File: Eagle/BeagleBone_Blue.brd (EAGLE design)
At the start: 86.4 x 54.6 mm, 128 parts, among them M1 JST_ZH_2, M2 JST_ZH_2, M3 JST_ZH_2, M4 JST_ZH_2, Q3 MOSFET-N, Q4 MOSFET-P, U1 MPU-9250

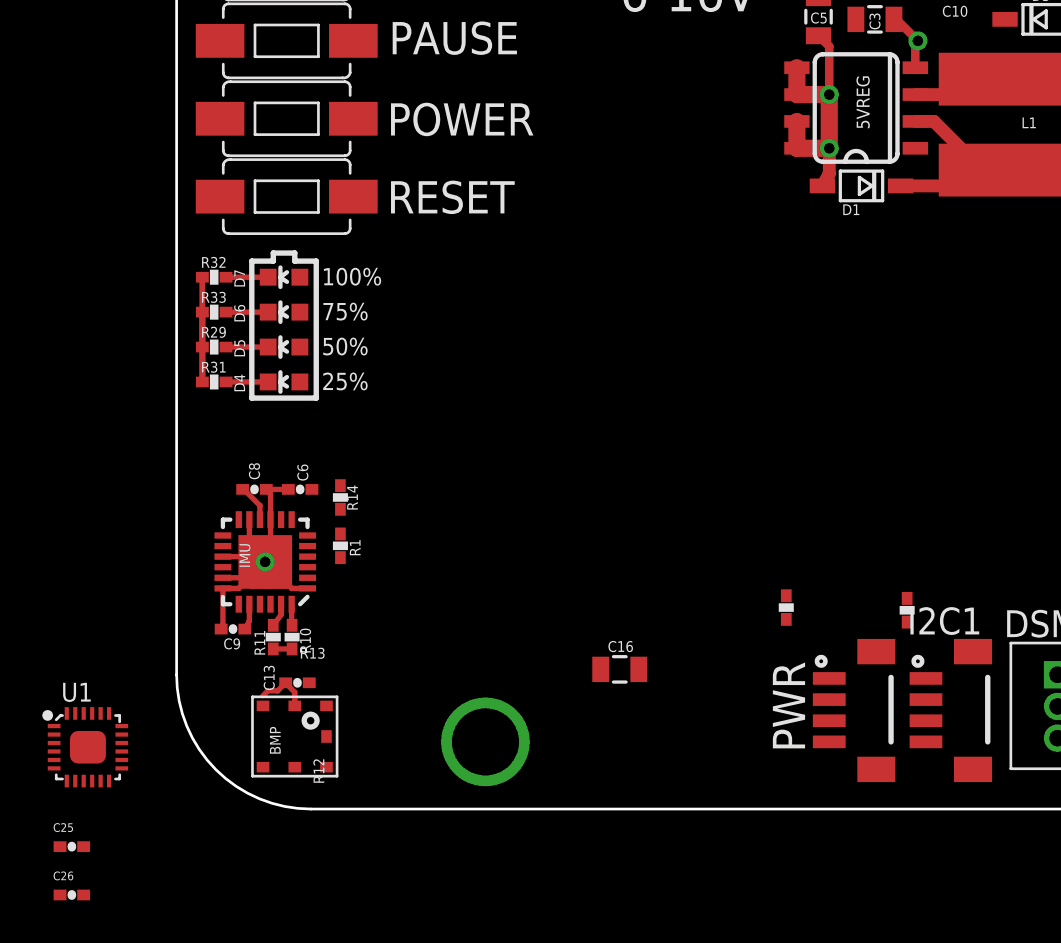
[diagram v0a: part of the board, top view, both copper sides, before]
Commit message: working on ERCs
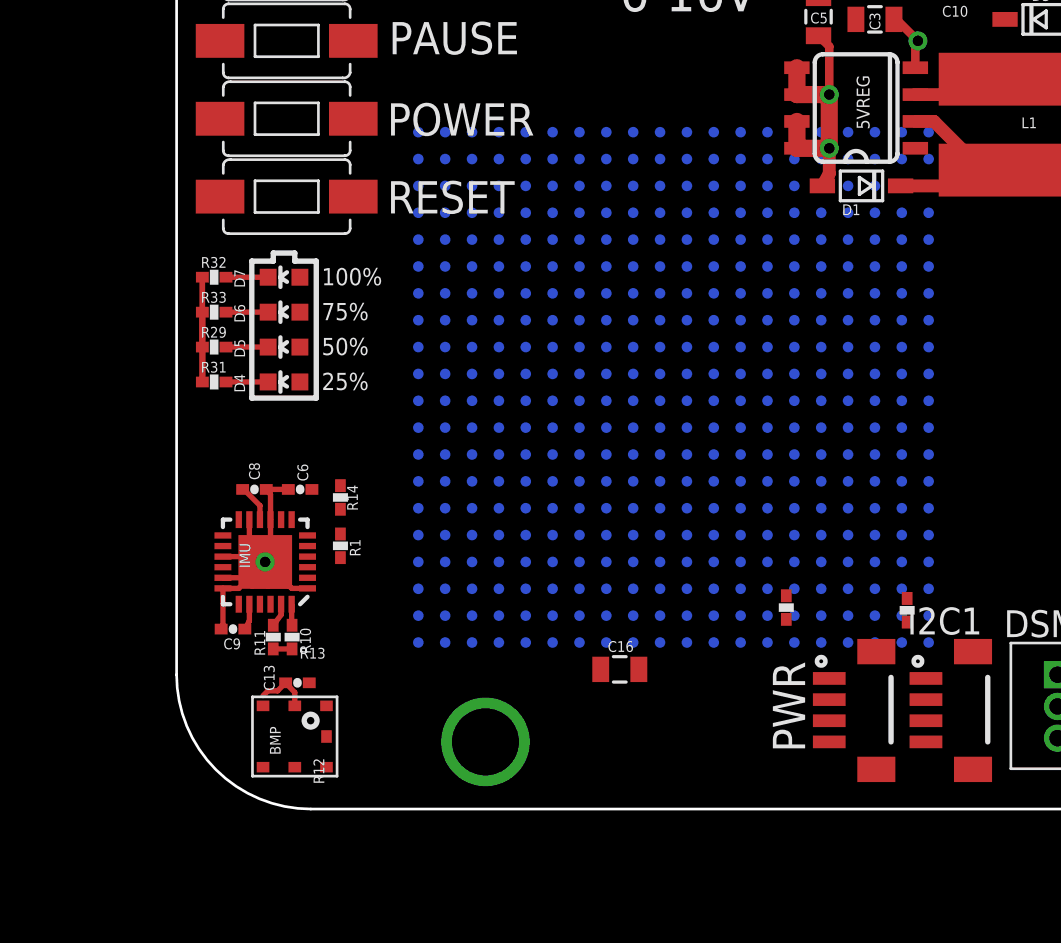
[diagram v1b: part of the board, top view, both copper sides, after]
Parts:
- removed C25, C26: 0.1uF, Strawson_Eagle_Lib:0402-CAP
- removed U1: MPU-9250, Strawson_Eagle_Lib:QFN24G-0.4-3X3MM
- added SIP: (no value), BeagleBone_Blue:OSD3358
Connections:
- removed net N$70: C26.2, U1.10
- net 3.3V: no longer C25.1, U1.1, U1.13, U1.8
- net GND: no longer C25.2, C26.1, U1.18, U1.20, U1.25, U1.9
- net I2C2_SCL: no longer U1.23
- net I2C2_SDA: no longer U1.24
- net IMU_INT: no longer U1.12

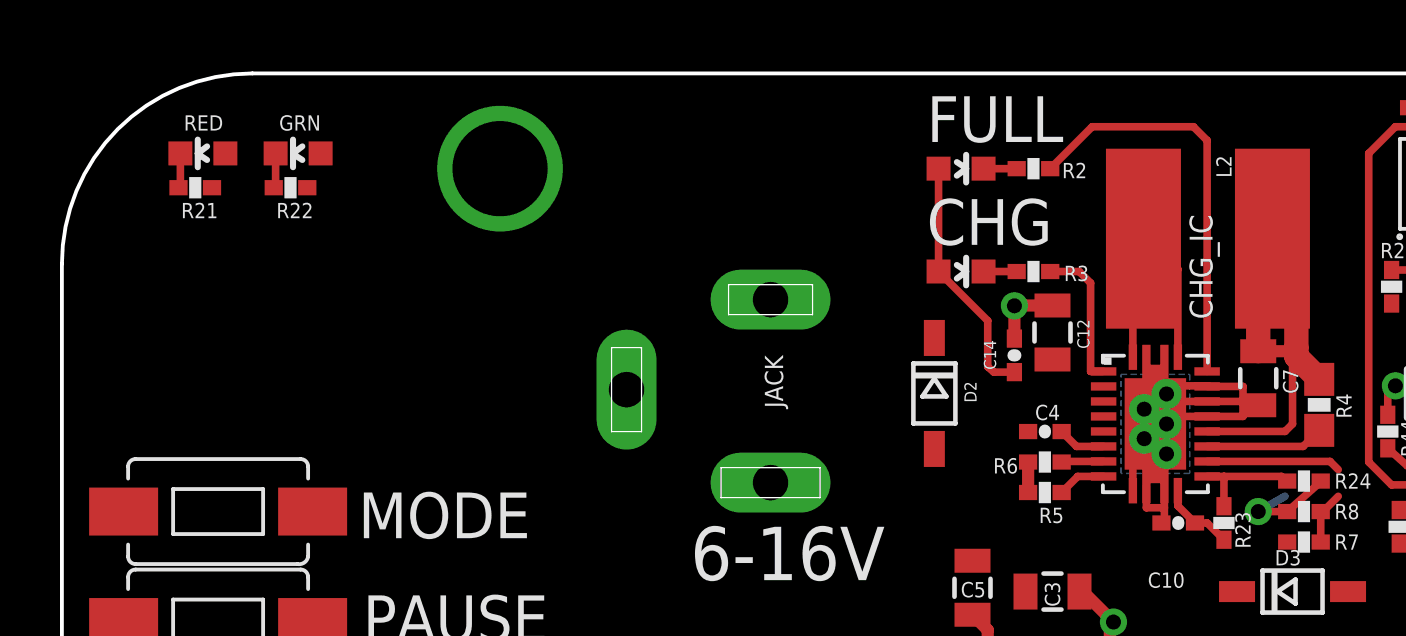
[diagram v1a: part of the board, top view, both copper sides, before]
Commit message: Fix some ERCs
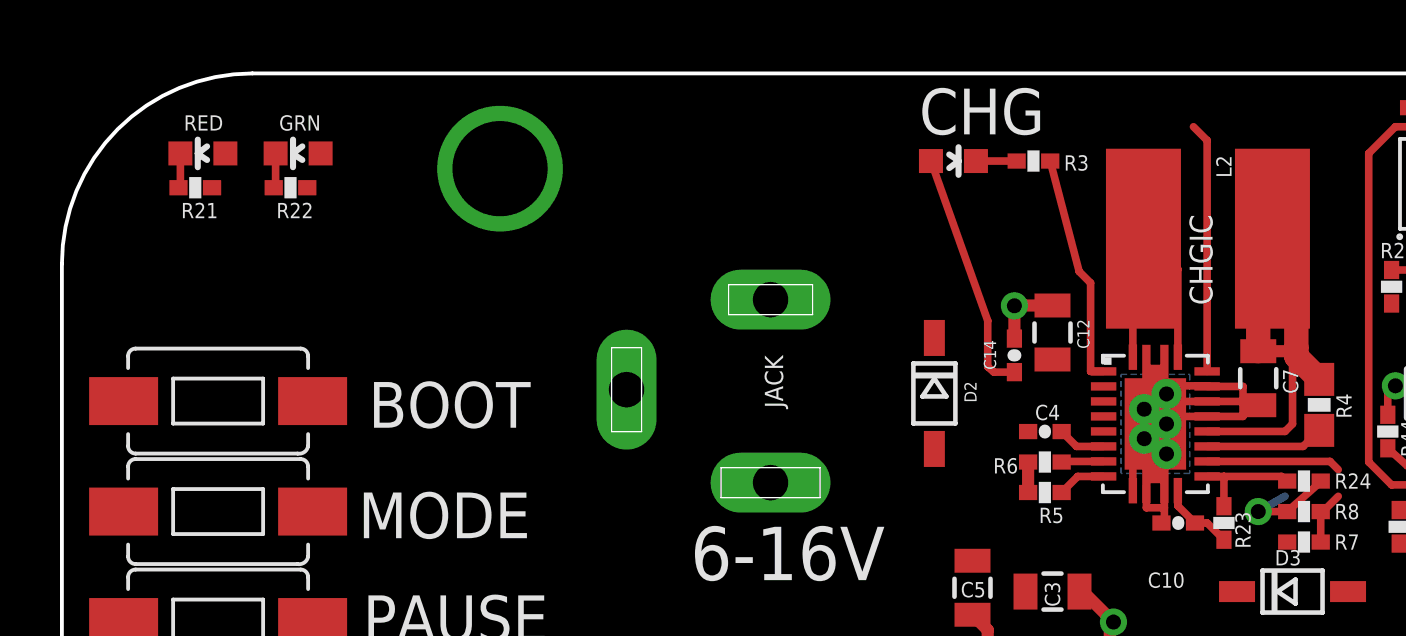
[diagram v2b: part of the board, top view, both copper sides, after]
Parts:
- removed FULL: GRN, SparkFun-LED:LED-0603
- removed R2: 698, Strawson_Eagle_Lib:0402-RES
- added BOOT: SWITCH-MOMENTARY-2-SMD-1101NE, SparkFun-Electromechanical:TACTILE-SWITCH-1101NE
- moved CHG 3.69 mm to (29.7, 51.7)
- moved R3 3.68 mm to (32.4, 51.7)
- renumbered CHG_IC to CHGIC
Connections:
- removed net N$9: FULL.C, R2.2
- net N$23: no longer R2.1
- net VCC: no longer FULL.A
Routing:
- net N$23: track 13.7 -> 8.34 mm
- net N$18: track 4.89 -> 7.73 mm
- net N$9: track 1.10 -> 0.00 mm

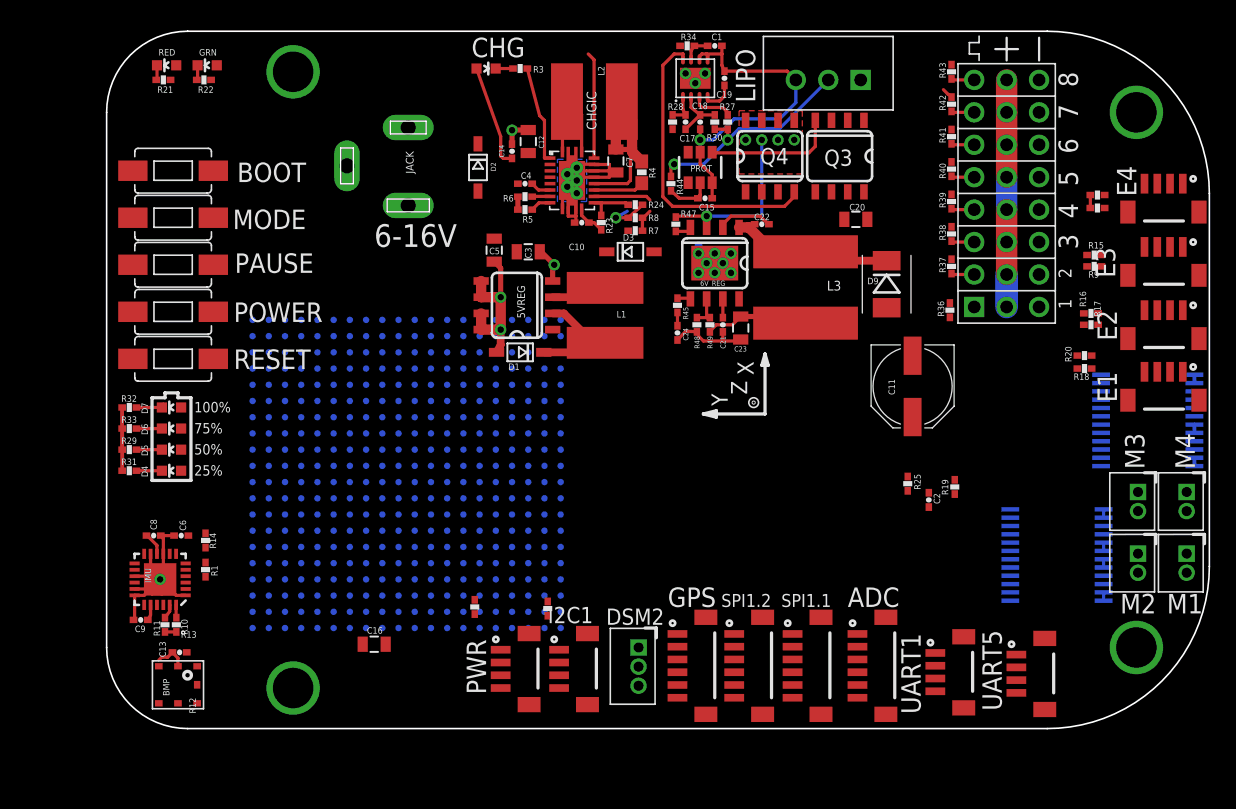
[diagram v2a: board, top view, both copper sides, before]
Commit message: Add uSD card
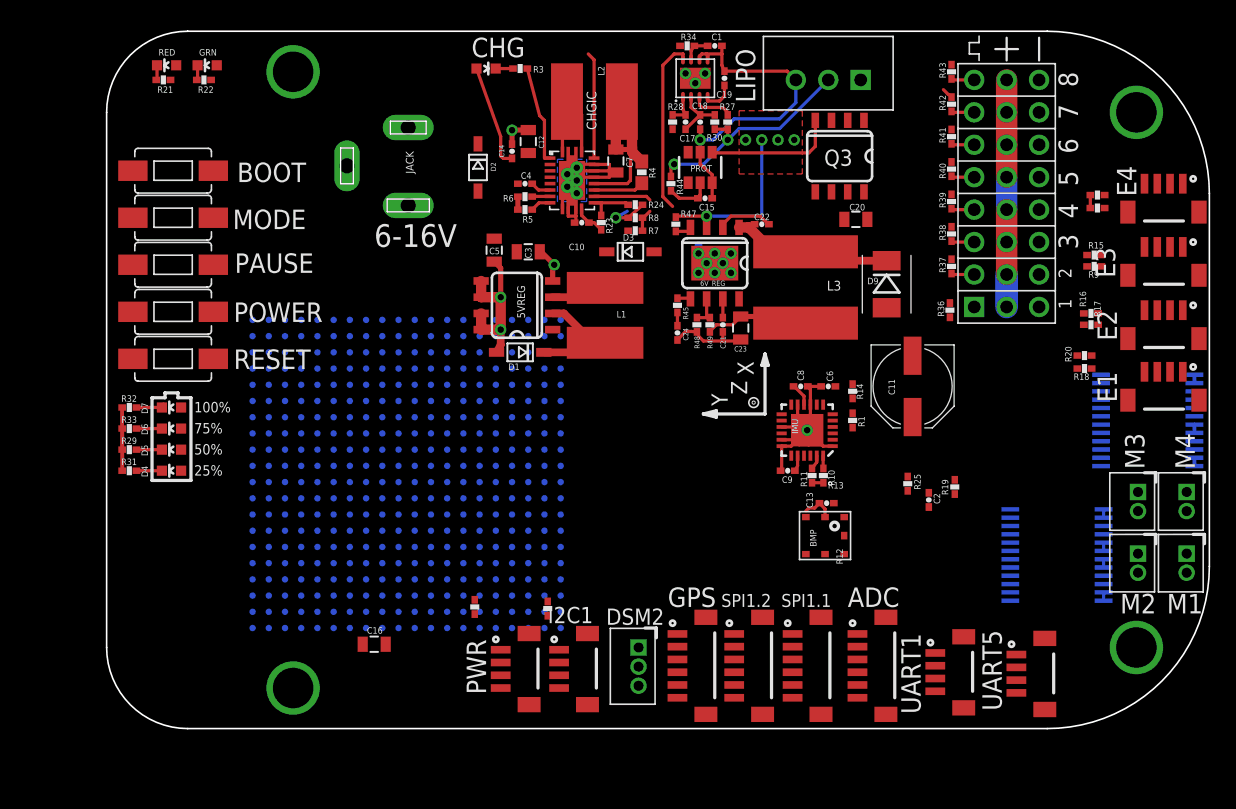
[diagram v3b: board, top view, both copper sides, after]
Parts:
- removed Q4: MOSFET-P, Strawson_Eagle_Lib:SO08-TIGHT
- moved BMP 52.0 mm to (56.3, 15.1)
- moved C13 52.0 mm to (56.4, 17.7)
- moved C6 52.0 mm to (56.5, 26.8)
- moved C8 52.0 mm to (54.4, 26.8)
- moved C9 52.0 mm to (53.3, 20.2)
- moved R1 52.0 mm to (58.4, 24.1)
- moved R10 52.0 mm to (56.1, 19.8)
- moved R14 52.0 mm to (58.4, 26.4)
- moved IMU 52.0 mm to (54.9, 23.4)
- moved R11 52.0 mm to (55.2, 19.8)
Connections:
- net CO: no longer Q4.4
- net GND: no longer Q4.5, Q4.6, Q4.7, Q4.8
- net N$21: no longer Q4.1, Q4.2, Q4.3
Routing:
- net CO: track 24.0 -> 13.7 mm

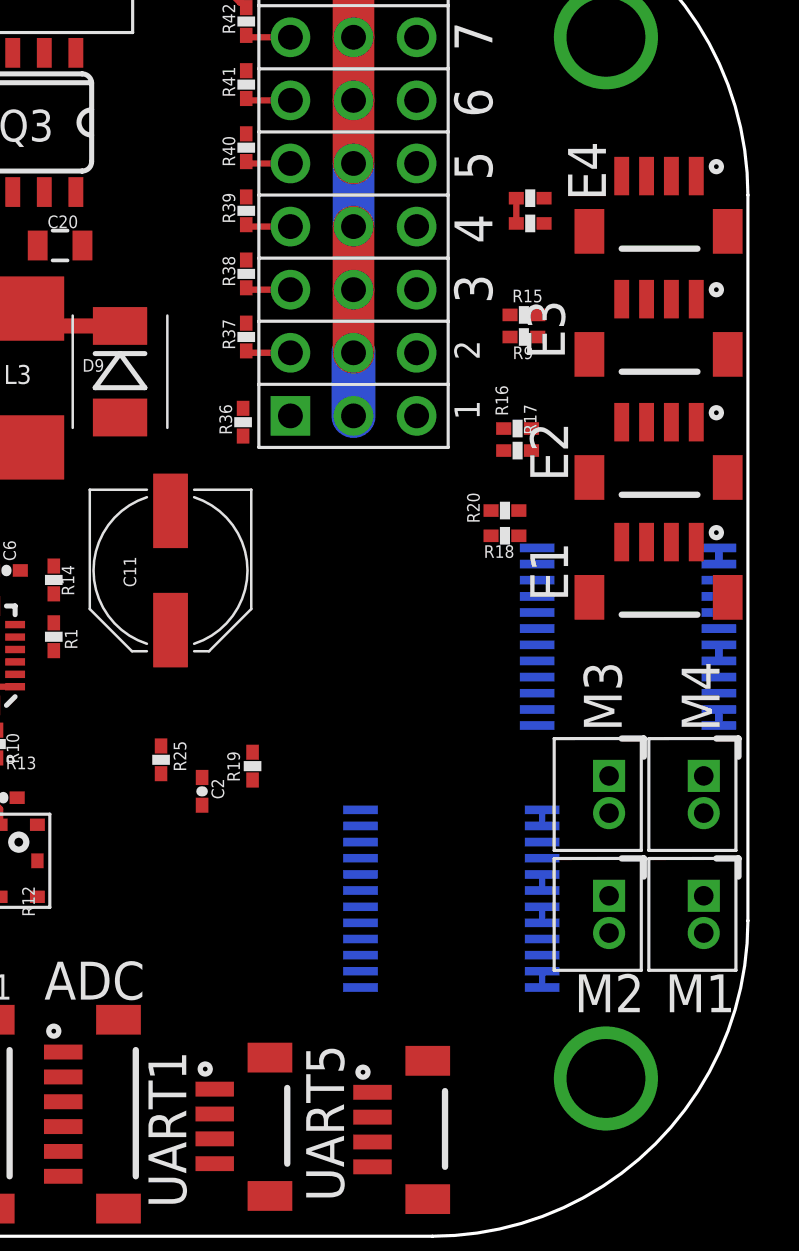
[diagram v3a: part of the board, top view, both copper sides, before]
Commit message: Place uSD card
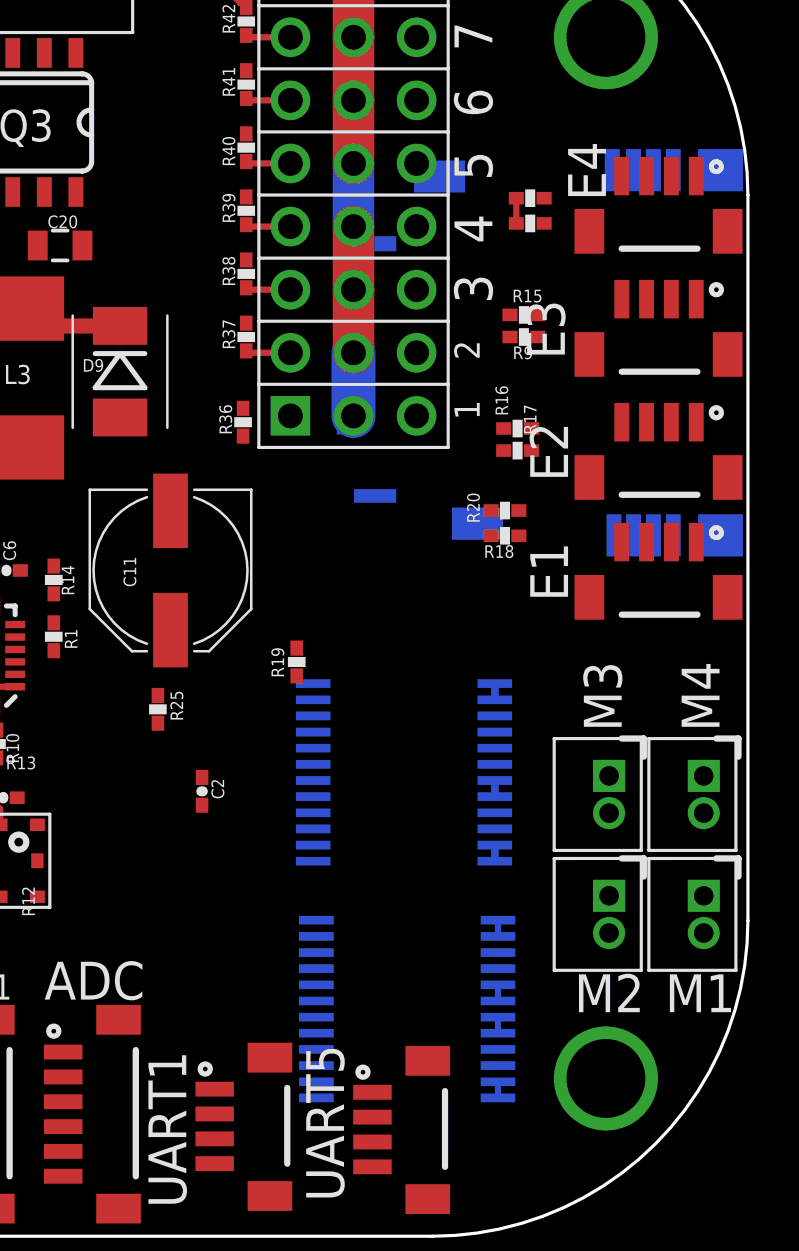
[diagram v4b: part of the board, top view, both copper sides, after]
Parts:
- added P10: (no value), SCHA5B0200:SCHA5B0200
- moved H2 10.5 mm to (72.5, 18.7)
- moved H1 4.79 mm to (72.6, 9.14)
- moved R19 4.55 mm to (68.2, 23.1)
- moved R25 2.04 mm to (62.6, 21.2)
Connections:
- net VCC: no longer R1.1

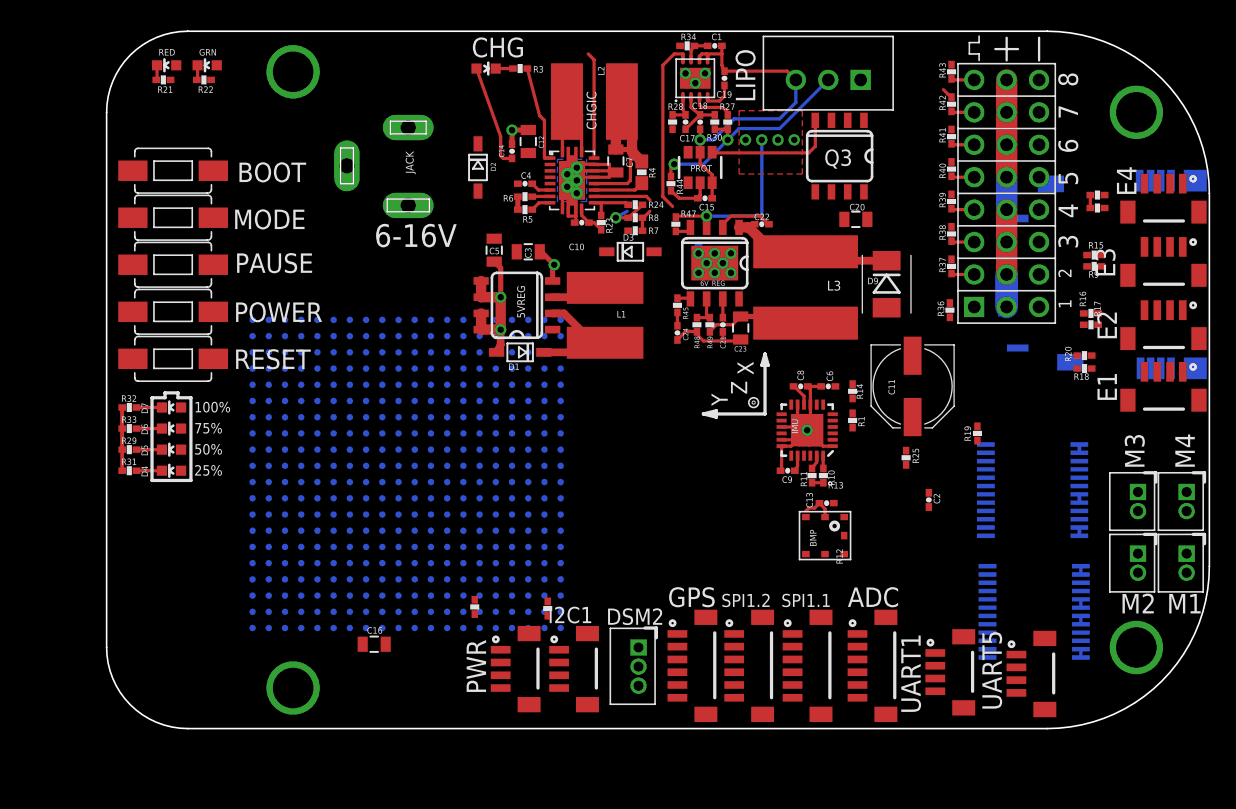
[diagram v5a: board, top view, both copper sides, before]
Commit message: Move uSD to long bottom side
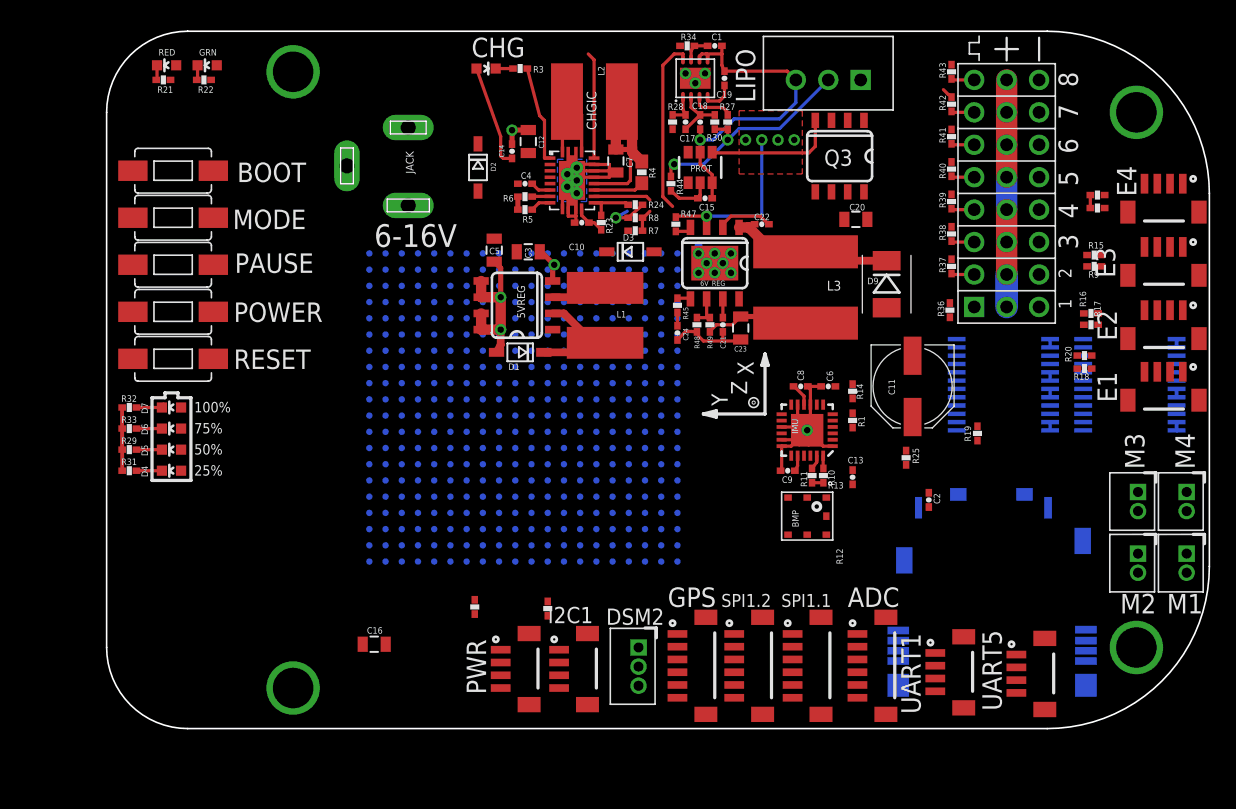
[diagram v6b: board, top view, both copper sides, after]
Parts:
- moved P10 48.5 mm to (80.8, -0.76), turned to 0 degrees
- moved H1 17.9 mm to (70.2, 26.9)
- moved H2 11.2 mm to (80.1, 26.9)
- moved SIP 10.5 mm to (32.6, 25.1)
- moved C13 2.87 mm to (58.4, 19.7), turned to 270 degrees
- moved BMP 2.07 mm to (54.9, 16.6)
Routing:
- net 3.3V: track 4.49 -> 1.91 mm
